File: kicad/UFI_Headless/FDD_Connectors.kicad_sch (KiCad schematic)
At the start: 6 parts, among them J6 FDD_34PIN, J7 AMIGA_FDD

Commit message: UFI Headless v0.4: J6 pin 6 DRATE via JP1, pin 3 GND/+5V via JP2
DRATE is driven by PF11 through the spare LS07 gate U7.11 -> U7.10 with
pull-up RN3.3; J6 pin 6 only sees it when solder jumper JP1 is bridged.
J6 pin 3 goes through JP2 (default 1-2 = GND, 2-3 = FDD_5V for PS/2 drives).
Firmware moves FDD_DRATE from PE6 to PF11.
DRC 0 violations, 0 unconnected, parity clean; fab outputs regenerated.
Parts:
- added JP1: DRATE, Jumper:SolderJumper-2_P1.3mm_Open_RoundedPad1.0x1.5mm, symbol Jumper:SolderJumper_2_Open
- added JP2: PIN3_GND/5V, Jumper:SolderJumper-3_P1.3mm_Bridged12_RoundedPad1.0x1.5mm, symbol Jumper:SolderJumper_3_Bridged12
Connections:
- net FDD_5V: now also JP2.3 (B)
- net GND: now also JP2.1 (A); no longer J6.3 (Pin_3)
- net FD_PIN6: now reaches J6.6 (Pin_6)
- net FD_PIN6: now also JP1.2 (B)
- new net FD_DRATE: JP1.1 (A)
- new net FD_PIN3: J6.3 (Pin_3), JP2.2 (C)
- no-connect marks 5 -> 4
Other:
- note added: "v0.4: JP1 open = J6 pin 6 unused, bridge = DRATE (3-mode drives). JP2 default 1-2 = pin 3 GND; 2-3 = +5V (fused FDD_5V) ONLY for PS/2 drives that take power on pin 3."

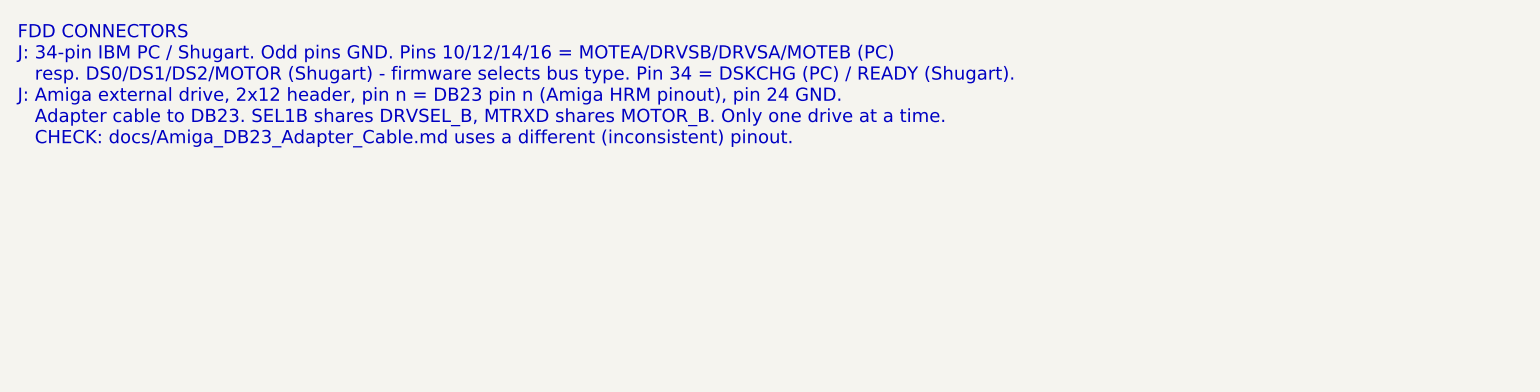
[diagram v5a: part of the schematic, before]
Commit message: Firmware 1.6: Shugart bus pin 34 = READY, no disk change line
Checked J6 against pinouts.ru 'Floppy Diskdrive pinout': the PC pinout matches pin for
pin; on the Shugart bus pin 34 is READY (not DSKCHG) and pin 2 is the drive's /DCD
output (ours is DENSITY, both open collector, not readable).
- DS0-DS3: ufi_drive_disk_changed() = false, ufi_drive_ready() reads pin 34
- USB floppy on the Shugart bus: no disk without READY (motor on), cached tracks are
  dropped when the motor stops (a swap goes unseen), detection retry 30 s
- floppy simulation passes for PC and Shugart bus
- README / schematic note: Shugart pin differences and the missing change detection
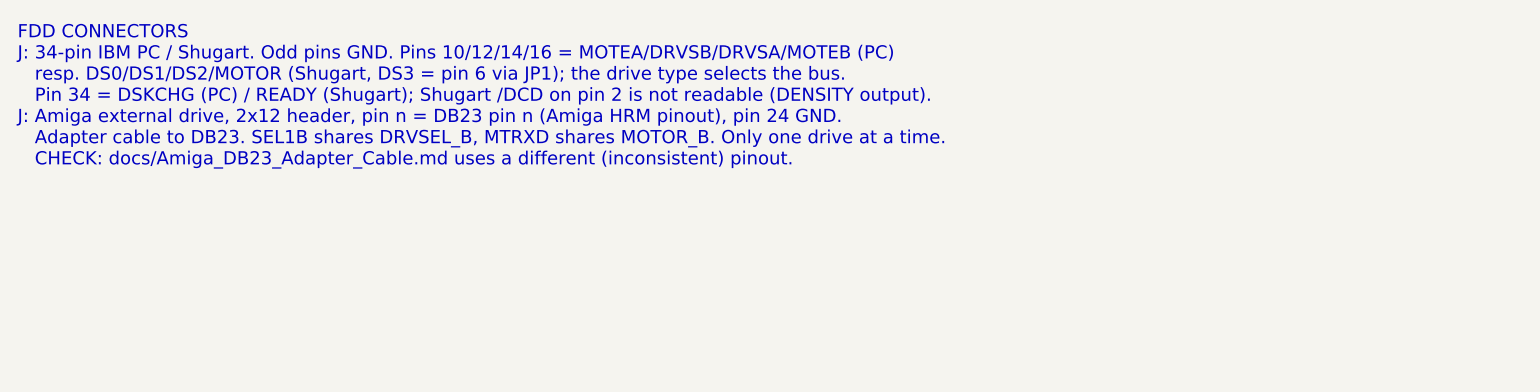
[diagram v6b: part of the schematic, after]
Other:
- note added: "FDD CONNECTORS J: 34-pin IBM PC / Shugart. Odd pins GND. Pins 10/12/14/16 = MOTEA/DRVSB/DRVSA/MOTEB (PC) resp. DS0/DS1/DS2/MOTOR (Shugart, DS3 = pin 6 via JP1); the drive type selects the bus. Pin 34 = DSKCHG (PC) / READY (Shugart); Shugart /DCD on pin 2 is not readable (DENSITY output). J: Amiga external drive, 2x12 header, pin n = DB23 pin n (Amiga HRM pinout), pin 24 GND. Adapter cable to DB23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"
- note removed: "FDD CONNECTORS J: 34-pin IBM PC / Shugart. Odd pins GND. Pins 10/12/14/16 = MOTEA/DRVSB/DRVSA/MOTEB (PC) resp. DS0/DS1/DS2/MOTOR (Shugart) - firmware selects bus type. Pin 34 = DSKCHG (PC) / READY (Shugart). J: Amiga external drive, 2x12 header, pin n = DB23 pin n (Amiga HRM pinout), pin 24 GND. Adapter cable to DB23. SEL1B shares DRVSEL_B, MTRXD shares MOTOR_B. Only one drive at a time. CHECK: d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"
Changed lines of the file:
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@@
 (paper "A3")
 (title_block (title "UFI Headless - FDD Connectors") (date "2026-10-05") (rev "0.1") (company "UFI Project"))
-(text "FDD CONNECTORS\nJ: 34-pin IBM PC / Shugart. Odd pins GND. Pins 10/12/14/16 = MOTEA/DRVSB/DRVSA/MOTEB (PC)\n   resp. DS0/DS1/DS2/MOTOR (Shugart) - firmware selects bus type. Pin 34 = DSKCHG (PC) / READY (Shugart).\nJ: Amiga external drive, 2x12 header, pin n = DB23 pin n (Amiga HRM pinout), pin 24 GND.\n   Adapter cable to DB23. SEL1B shares DRVSEL_B, MTRXD shares MOTOR_B. Only one drive at a time.\n   CHECK: docs/Amiga_DB23_Adapter_Cable.md uses a different (inconsistent) pinout." (exclude_from_sim no) (at 20 20 0) (effects (font (size 1.5 1.5)) (justify left top)))
+(text "FDD CONNECTORS\nJ: 34-pin IBM PC / Shugart. Odd pins GND. Pins 10/12/14/16 = MOTEA/DRVSB/DRVSA/MOTEB (PC)\n   resp. DS0/DS1/DS2/MOTOR (Shugart, DS3 = pin 6 via JP1); the drive type selects the bus.\n   Pin 34 = DSKCHG (PC) / READY (Shugart); Shugart /DCD on pin 2 is not readable (DENSITY output).\nJ: Amiga external drive, 2x12 header, pin n = DB23 pin n (Amiga HRM pinout), pin 24 GND.\n   Adapter cable to DB23. SEL1B shares DRVSEL_B, MTRXD shares MOTOR_B. Only one drive at a time.\n   CHECK: docs/Amiga_DB23_Adapter_Cable.md uses a different (inconsistent) pinout." (exclude_from_sim no) (at 20 20 0) (effects (font (size 1.5 1.5)) (justify left top)))
 (wire (pts (xy 83.82 88.9) (xy 81.28 88.9)) (stroke (width 0) (type default)))
 (wire (pts (xy 96.52 88.9) (xy 99.06 88.9)) (stroke (width 0) (type default)))
